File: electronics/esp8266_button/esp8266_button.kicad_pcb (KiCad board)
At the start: 2 copper layers, 40 x 50 mm, 40 parts, among them J1 CONN_01X06, J2 CONN_01X06, J3 CONN_01X08, J4 CONN_01X08, M1 BMP180_Breakout, P1 OSHW, P2 M3 Hole, P3 M3 Hole, P4 Fid, P5 Fid, P6 Fid, Q1 Q_NMOS_GSD, Q2 Q_PMOS_GSD, SW1 SW_Push, SW2 SW_Push, SW3 SW_Push, U1 MCP1703A-3302/MB, U2 ESP-12

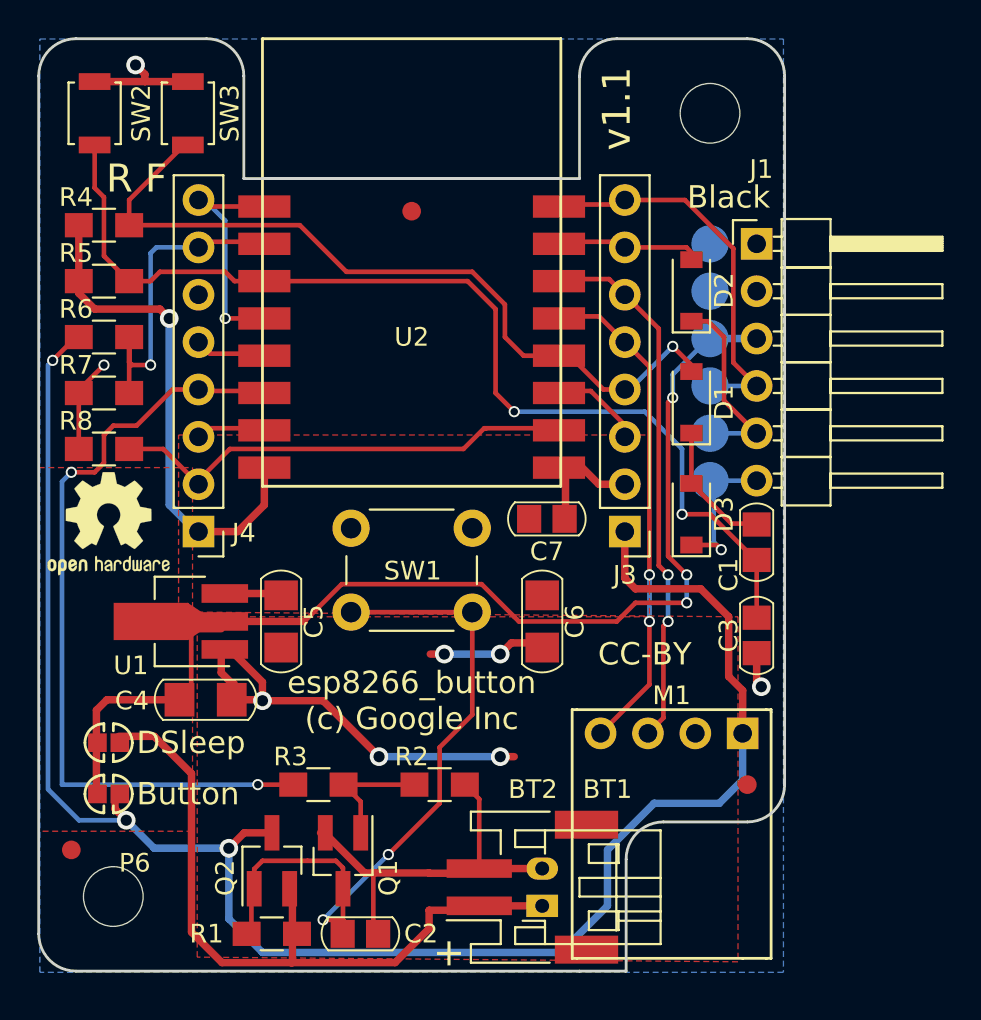
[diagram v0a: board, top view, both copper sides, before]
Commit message: Move around topmost resistor a bit
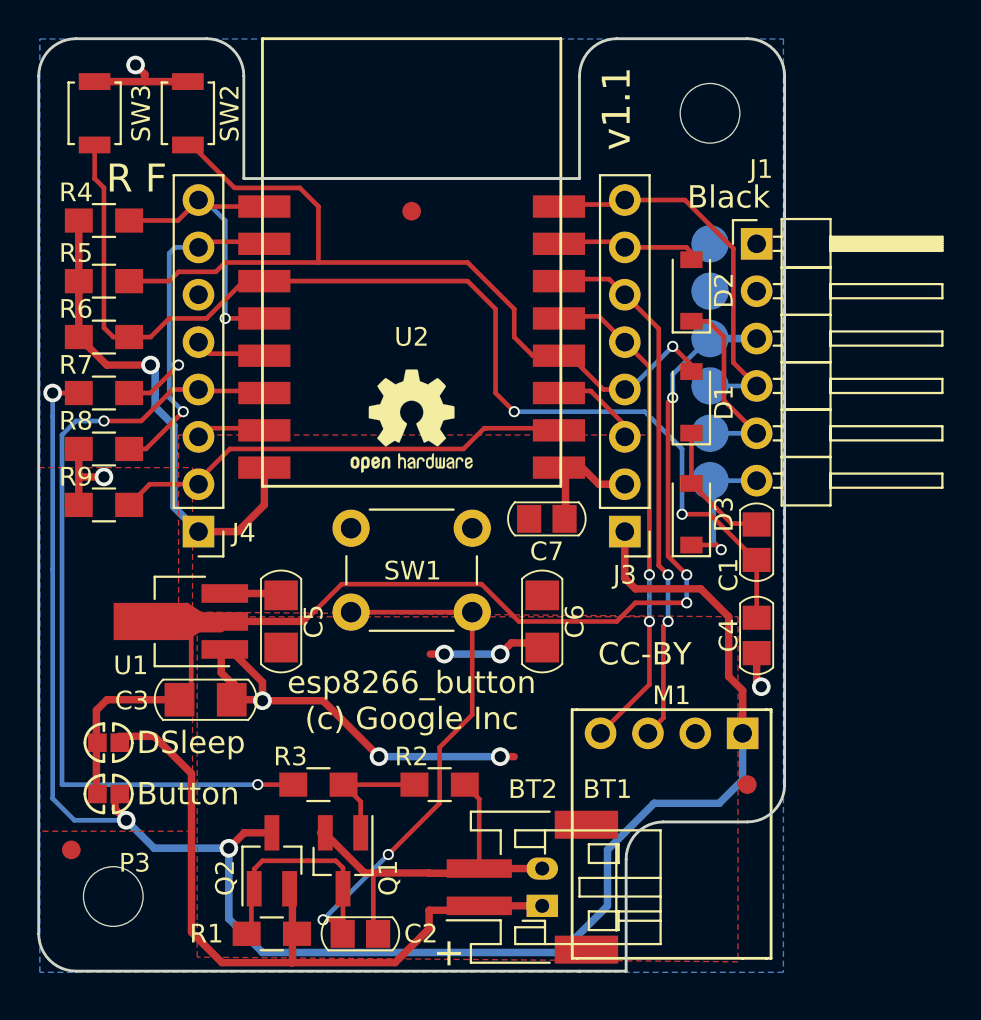
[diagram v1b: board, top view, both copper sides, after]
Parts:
- added R4: 10k, Resistors_SMD:R_0805_HandSoldering, F.Cu at (137.8, 87.8)
- moved P4 17.2 mm to (154.3, 98.6)
- moved R5 3.00 mm to (137.8, 91.1)
- moved R6 3.00 mm to (137.8, 94.1)
- moved R7 3.00 mm to (137.8, 97.1)
- moved R8 3.00 mm to (137.8, 100.1)
- moved R9 3.00 mm to (137.8, 103.1)
- renumbered C4 to C3, C3 to C4, P4 to P1, P5 to P2, P6 to P3, P1 to P4, P2 to P5, P3 to P6, R4 to R5, R5 to R6, R6 to R7, R7 to R8, R8 to R9, SW3 to SW2, SW2 to SW3
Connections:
- net /RESET renamed RESET
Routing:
- net GPIO0: track 44.4 -> 49.7 mm
- net /ADC: track 19.5 -> 24.1 mm, vias 1 -> 2
- net CH_PD: track 56.1 -> 60.5 mm
- net RESET: track 13.3 -> 17.5 mm
- net BATTMON: track 96.2 -> 93.9 mm
- net +3V3: track 30.8 -> 32.1 mm
- net GND: track 71.1 -> 71.9 mm
- net GPIO12: track 44.5 -> 45.0 mm
